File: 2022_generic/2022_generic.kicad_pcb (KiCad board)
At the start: 2 copper layers, 50.8 x 43.2 mm, 17 parts, among them J1 Screw_Terminal_01x02, J2 Programming Connector, SW1 6mm tactile button, U1 PIC16LF15313

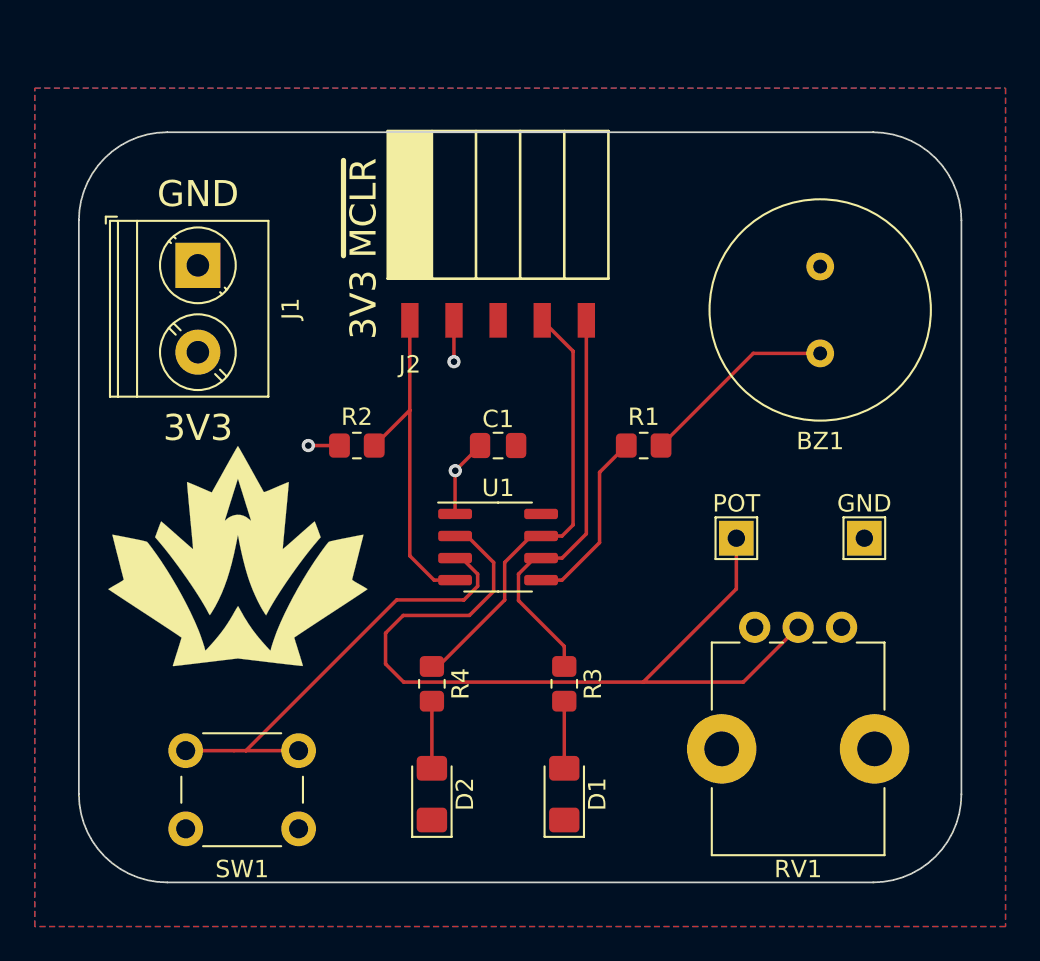
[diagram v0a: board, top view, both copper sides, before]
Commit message: Add mounting hole, move test points, generate pdf and gerbers
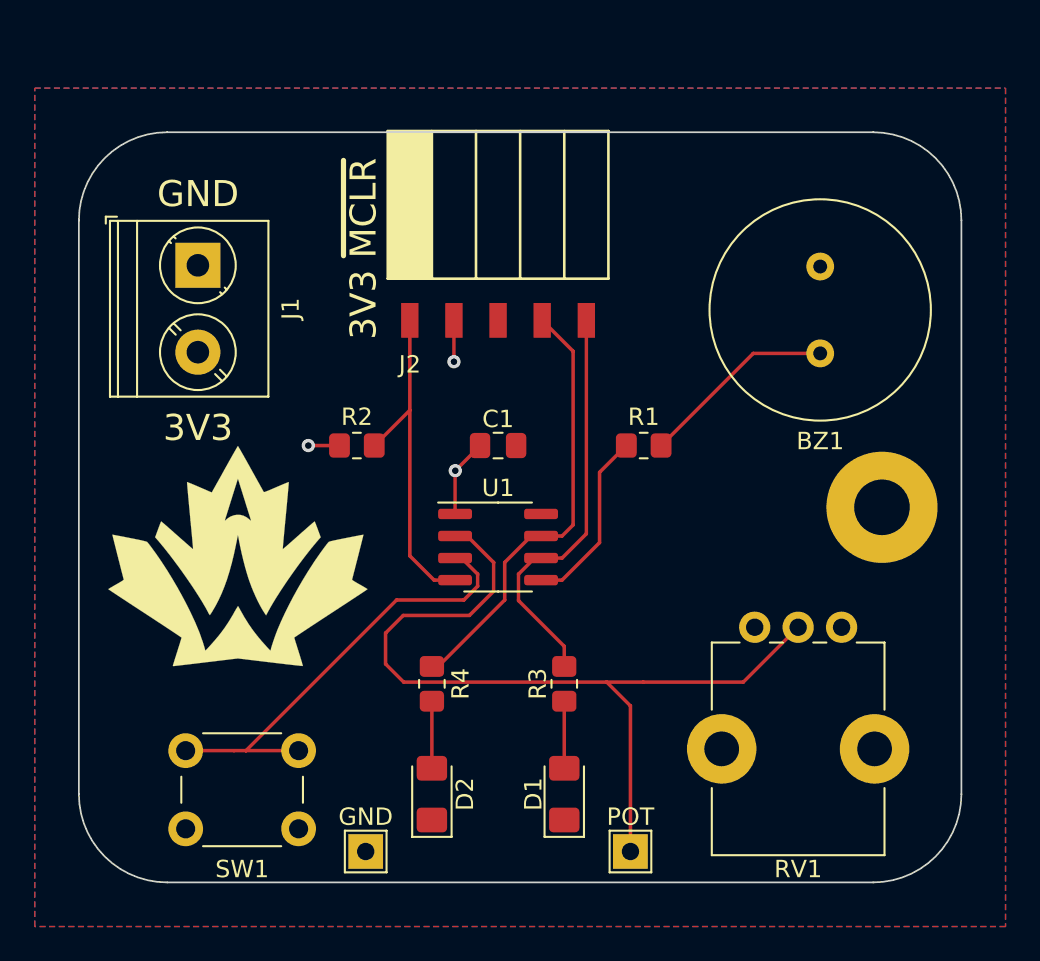
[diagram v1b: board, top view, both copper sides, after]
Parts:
- added REF**: MountingHole_3.2mm_M3_Pad, MountingHole:MountingHole_3.2mm_M3_Pad, F.Cu at (180.8, 118.1)
- moved GND 33.9 mm to (151.1, 137.9)
- moved POT 19.0 mm to (166.4, 137.9)
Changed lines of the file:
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@@
   (net 11 "Net-(SW1-Pad1)")
   (footprint "TestPoint:TestPoint_THTPad_2.0x2.0mm_Drill1.0mm" (layer "F.Cu")
-    (at 172.466 119.888)
+    (at 166.37 137.922)
     (descr "THT rectangular pad as test Point, square 2.0mm_Drill1.0mm  side length, hole diameter 1.0mm")
     (tags "test point THT pad rectangle square")
@@
   )
   (footprint "TestPoint:TestPoint_THTPad_2.0x2.0mm_Drill1.0mm" (layer "F.Cu")
-    (at 179.832 119.888)
+    (at 151.13 137.922)
     (descr "THT rectangular pad as test Point, square 2.0mm_Drill1.0mm  side length, hole diameter 1.0mm")
     (tags "test point THT pad rectangle square")
@@
     (property "Sheetname" "")
     (attr smd)
-    (fp_text reference "R3" (at 0 -1.65 90) (layer "F.SilkS")
+    (fp_text reference "R3" (at 0 1.524 90) (layer "F.SilkS")
       (effects (font (size 1 1) (thickness 0.15)))
     )
@@
     )
   )
+  (footprint "MountingHole:MountingHole_3.2mm_M3_Pad" (layer "F.Cu")
+    (at 180.848 118.11)
+    (descr "Mounting Hole 3.2mm, M3")
+    (tags "mounting hole 3.2mm m3")
+    (attr exclude_from_pos_files exclude_from_bom)
+    (fp_text reference "REF**" (at 0 -4.2) (layer "F.SilkS") hide
+      (effects (font (size 1 1) (thickness 0.15)))
+    )
+    (fp_text value "MountingHole_3.2mm_M3_Pad" (at 0 4.2) (layer "F.Fab")
+      (effects (font (size 1 1) (thickness 0.15)))
+    )
+    (fp_text user "${REFERENCE}" (at 0 0) (layer "F.Fab")
+      (effects (font (size 1 1) (thickness 0.15)))
+    )
+    (fp_circle (center 0 0) (end 3.2 0) (layer "Cmts.User") (width 0.15) (fill none))
+    (fp_circle (center 0 0) (end 3.45 0) (layer "F.CrtYd") (width 0.05) (fill none))
+    (pad "1" thru_hole circle (at 0 0) (size 6.4 6.4) (drill 3.2) (layers *.Cu *.Mask))
+  )
   (footprint "Resistor_SMD:R_0805_2012Metric_Pad1.20x1.40mm_HandSolder" (layer "F.Cu")
     (at 150.622 114.554)
@@
     (property "Sheetname" "")
     (attr smd)
-    (fp_text reference "D1" (at 0 1.905 90) (layer "F.SilkS")
+    (fp_text reference "D1" (at 0 -1.778 90) (layer "F.SilkS")
       (effects (font (size 1 1) (thickness 0.15)))
     )
@@
   (segment (start 157.099 124.333) (end 153.289 124.333) (width 0.2032) (layer "F.Cu") (net 10))
   (segment (start 152.273 125.349) (end 152.273 127.127) (width 0.2032) (layer "F.Cu") (net 10))
+  (segment (start 153.3176 128.1716) (end 165.0016 128.1716) (width 0.2032) (layer "F.Cu") (net 10))
   (segment (start 172.8644 128.1716) (end 176.022 125.014) (width 0.2032) (layer "F.Cu") (net 10))
-  (segment (start 172.466 122.809) (end 167.1034 128.1716) (width 0.2032) (layer "F.Cu") (net 10))
   (segment (start 156.972 119.761) (end 158.496 121.285) (width 0.2032) (layer "F.Cu") (net 10))
+  (segment (start 165.0016 128.1716) (end 167.1034 128.1716) (width 0.2032) (layer "F.Cu") (net 10))
+  (segment (start 166.37 137.922) (end 166.37 129.54) (width 0.2032) (layer "F.Cu") (net 10))
   (segment (start 158.496 121.285) (end 158.496 122.936) (width 0.2032) (layer "F.Cu") (net 10))
-  (segment (start 153.3176 128.1716) (end 167.1034 128.1716) (width 0.2032) (layer "F.Cu") (net 10))
-  (segment (start 172.466 119.888) (end 172.466 122.809) (width 0.2032) (layer "F.Cu") (net 10))
   (segment (start 153.289 124.333) (end 152.273 125.349) (width 0.2032) (layer "F.Cu") (net 10))
   (segment (start 152.273 127.127) (end 153.3176 128.1716) (width 0.2032) (layer "F.Cu") (net 10))
   (segment (start 167.1034 128.1716) (end 172.8644 128.1716) (width 0.2032) (layer "F.Cu") (net 10))
   (segment (start 156.275 119.761) (end 156.972 119.761) (width 0.2032) (layer "F.Cu") (net 10))
+  (segment (start 166.37 129.54) (end 165.0016 128.1716) (width 0.2032) (layer "F.Cu") (net 10))
   (segment (start 158.496 122.936) (end 157.099 124.333) (width 0.2032) (layer "F.Cu") (net 10))
   (segment (start 157.575 122.647751) (end 156.778751 123.444) (width 0.2032) (layer "F.Cu") (net 11))
